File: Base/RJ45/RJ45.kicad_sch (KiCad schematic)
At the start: 40 parts, among them J1 Barrel_Jack_Switch, J2 AudioJack2_Ground, J3 AudioJack2_Ground, J4 RJ45_LED_Shielded, T1 TLINE, U2 OPA1656

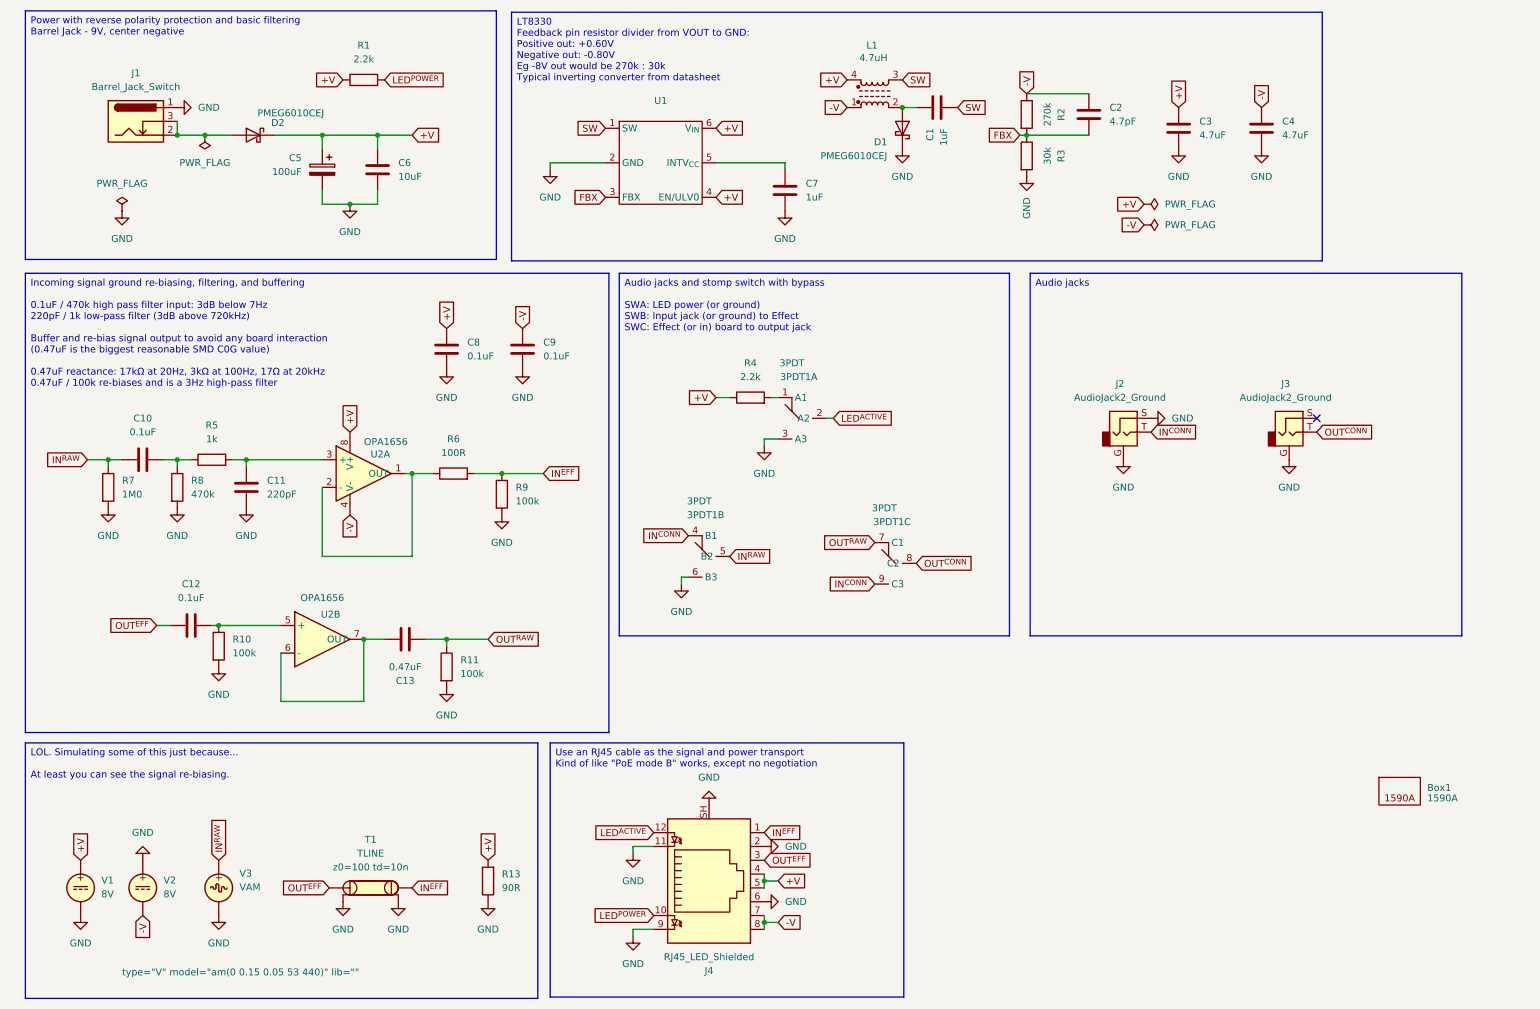
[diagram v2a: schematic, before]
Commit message: Update the RJ45 boards
So I'm doing two different cable versions in parallel to see which I
like better.  The "passive base board" version uses USB-C connectors and
really doesn't do anything at all but convert the power, stomp switch
and audio connectors to one single cable.  So the effects board is
supposed to do everything that is actually signal-related, including
generating its own reference voltages etc.

In contrast, the RJ45 board is "active", and also generates a negative
power rail.  That doesn't help the existing effects boards, but it means
that any boards actively designed for this have all the voltages
(assuming +-9V and GND works for them), and don't need to rebias signals
etc.

Do I know which board - if any - I'm actually going to develop further?
No.  They may both be garbage.

Signed-off-by: Linus Torvalds <torvalds@linux-foundation.org>
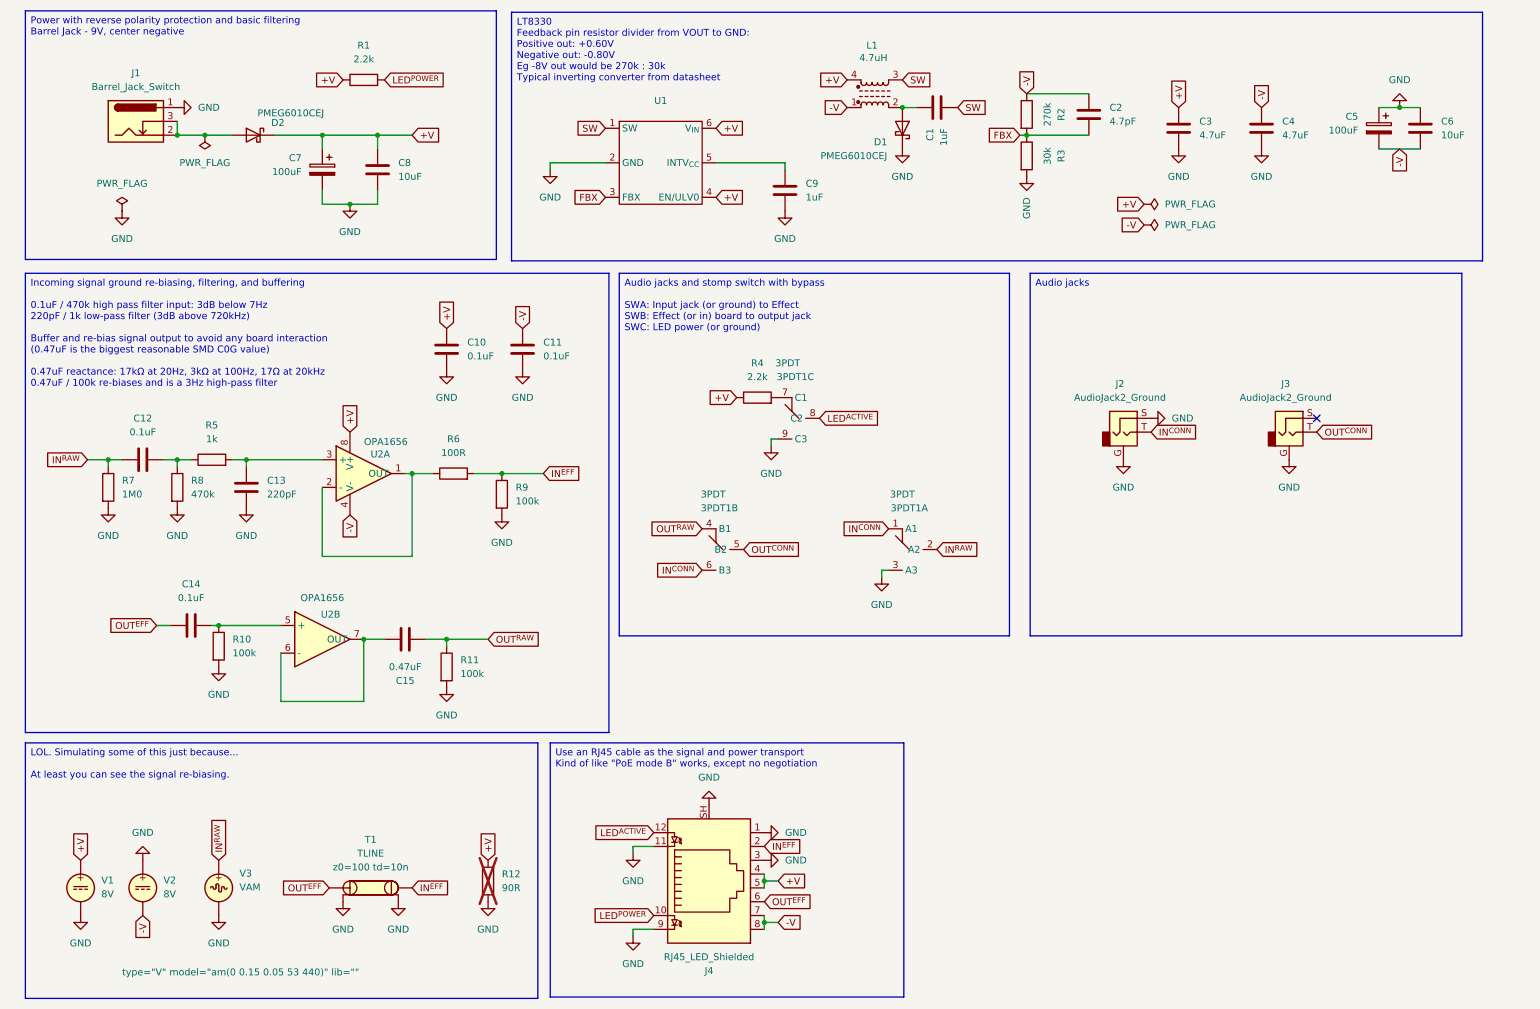
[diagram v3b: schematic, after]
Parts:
- removed Box1: 1590A, Mylib:1590A, symbol Mylib:Enclosure_1590A
- added C5: 100uF, Capacitor_THT:CP_Radial_D8.0mm_P3.50mm, symbol Device:C_Polarized
- added C6: 10uF, Capacitor_SMD:C_1206_3216Metric_Pad1.33x1.80mm_HandSolder, symbol Device:C
- R12: renamed from R13; now not fitted
- V3: now left out of the parts list
- renumbered C8 to C10, C9 to C11, C10 to C12, C11 to C13, C12 to C14, C13 to C15, C5 to C7, C6 to C8, C7 to C9
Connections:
- net -V: now also C5.2, C6.2
- net GND: now also 3PDT1.9 (C3), J4.1, J4.3, C5.1, C6.1; no longer 3PDT1.6 (B3), J4.2, J4.6
- net IN^{CONN}: now also 3PDT1.1 (A1), 3PDT1.6 (B3); no longer 3PDT1.4 (B1), 3PDT1.9 (C3)
- net IN^{EFF}: now also J4.2; no longer J4.1
- net IN^{RAW}: now also 3PDT1.2 (A2); no longer 3PDT1.5 (B2)
- net LED^{ACTIVE}: now also 3PDT1.8 (C2); no longer 3PDT1.2 (A2)
- net OUT^{CONN}: now also 3PDT1.5 (B2); no longer 3PDT1.8 (C2)
- net OUT^{EFF}: now also J4.6; no longer J4.3
- net OUT^{RAW}: now also 3PDT1.4 (B1); no longer 3PDT1.7 (C1)
- net at R4.2: now also 3PDT1.7 (C1); no longer 3PDT1.1 (A1)
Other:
- moved on the sheet: 3PDT1A, 3PDT1B, 3PDT1C, R4
